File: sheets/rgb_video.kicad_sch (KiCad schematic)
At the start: 51 parts, among them CN3 DIN-8, U32 CXA1145P

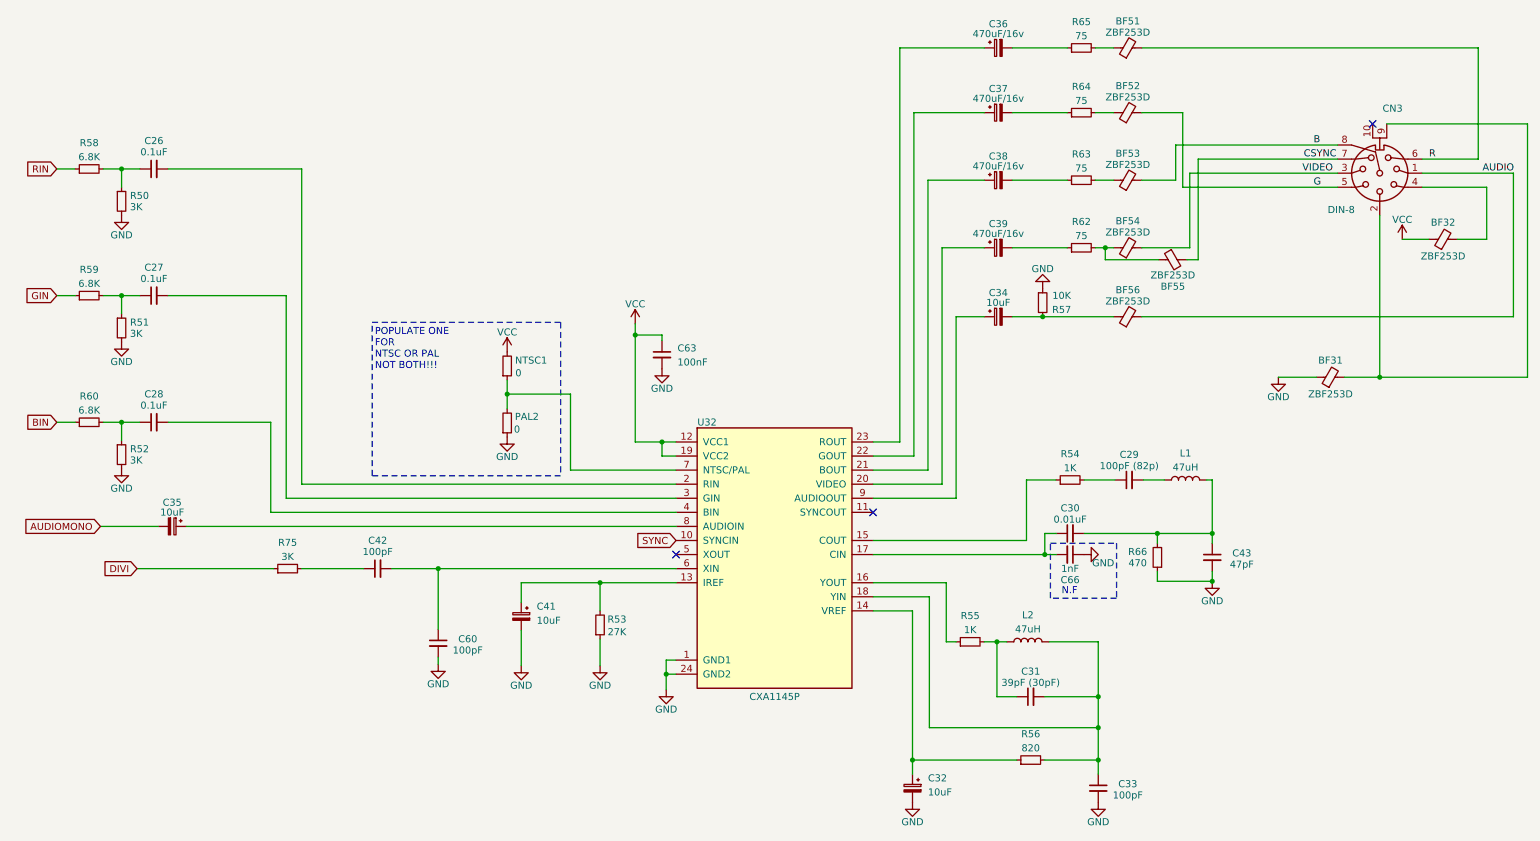
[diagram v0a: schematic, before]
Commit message: Updated to Kicad 10
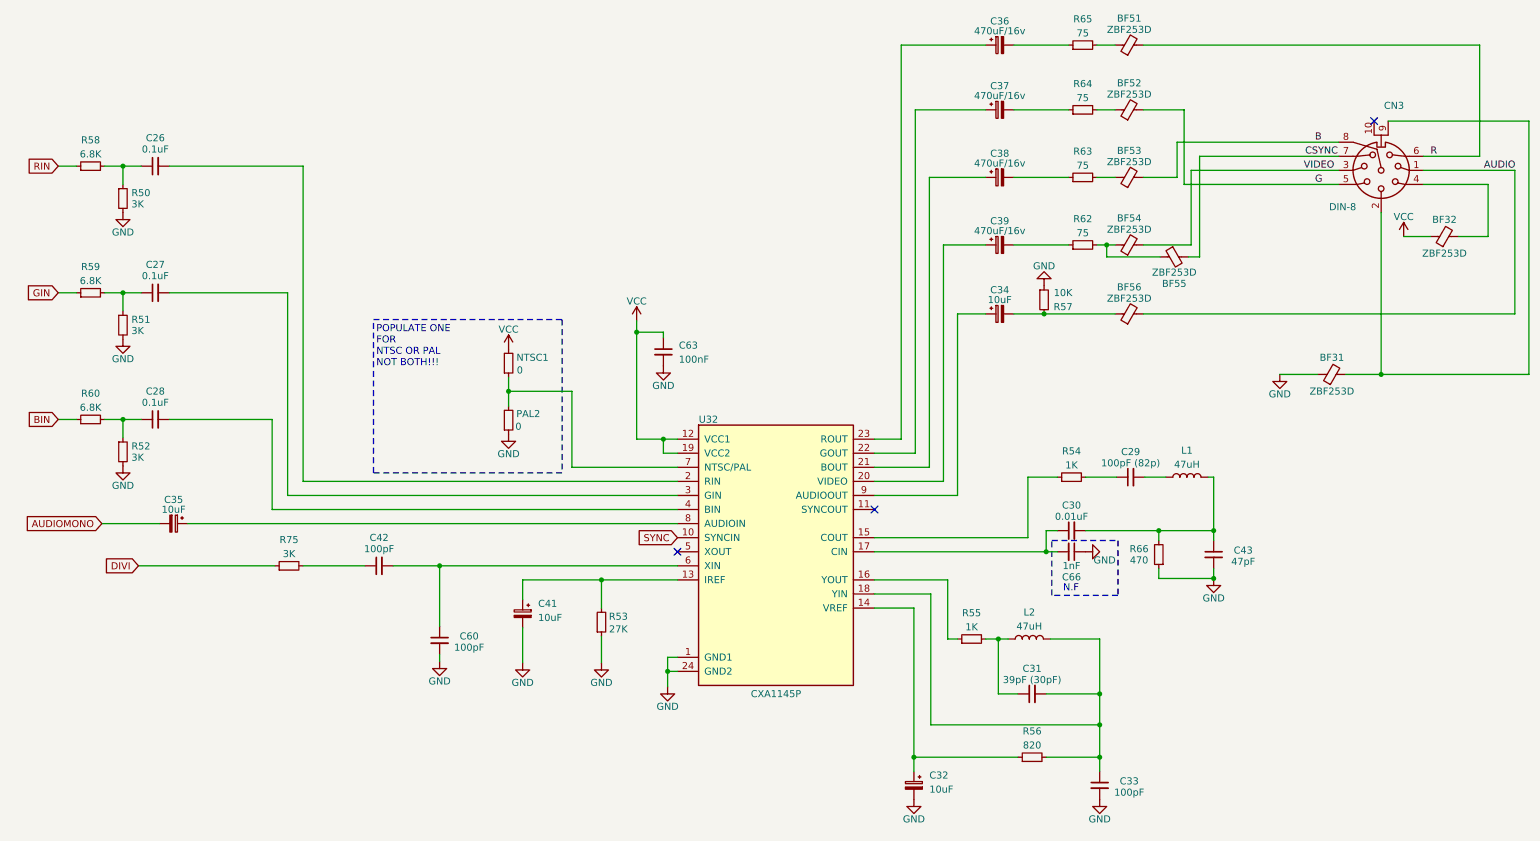
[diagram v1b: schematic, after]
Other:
- moved on the sheet: BF31, BF32, BF51, BF52, BF53, BF54, BF55, BF56, C26, C27, C28, C29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
